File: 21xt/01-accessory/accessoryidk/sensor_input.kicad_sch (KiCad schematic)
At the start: 25 parts, among them IC5 INA821IDGKT, IC6 TXB0108PWR, IC8 INA821IDGKT, IC9 INA821IDGKT, J2 5747847-6, J3 Conn_01x05, J4 Conn_01x06, J5 Conn_01x05, J6 Conn_01x05, J7 Conn_01x06, J8 Conn_01x05

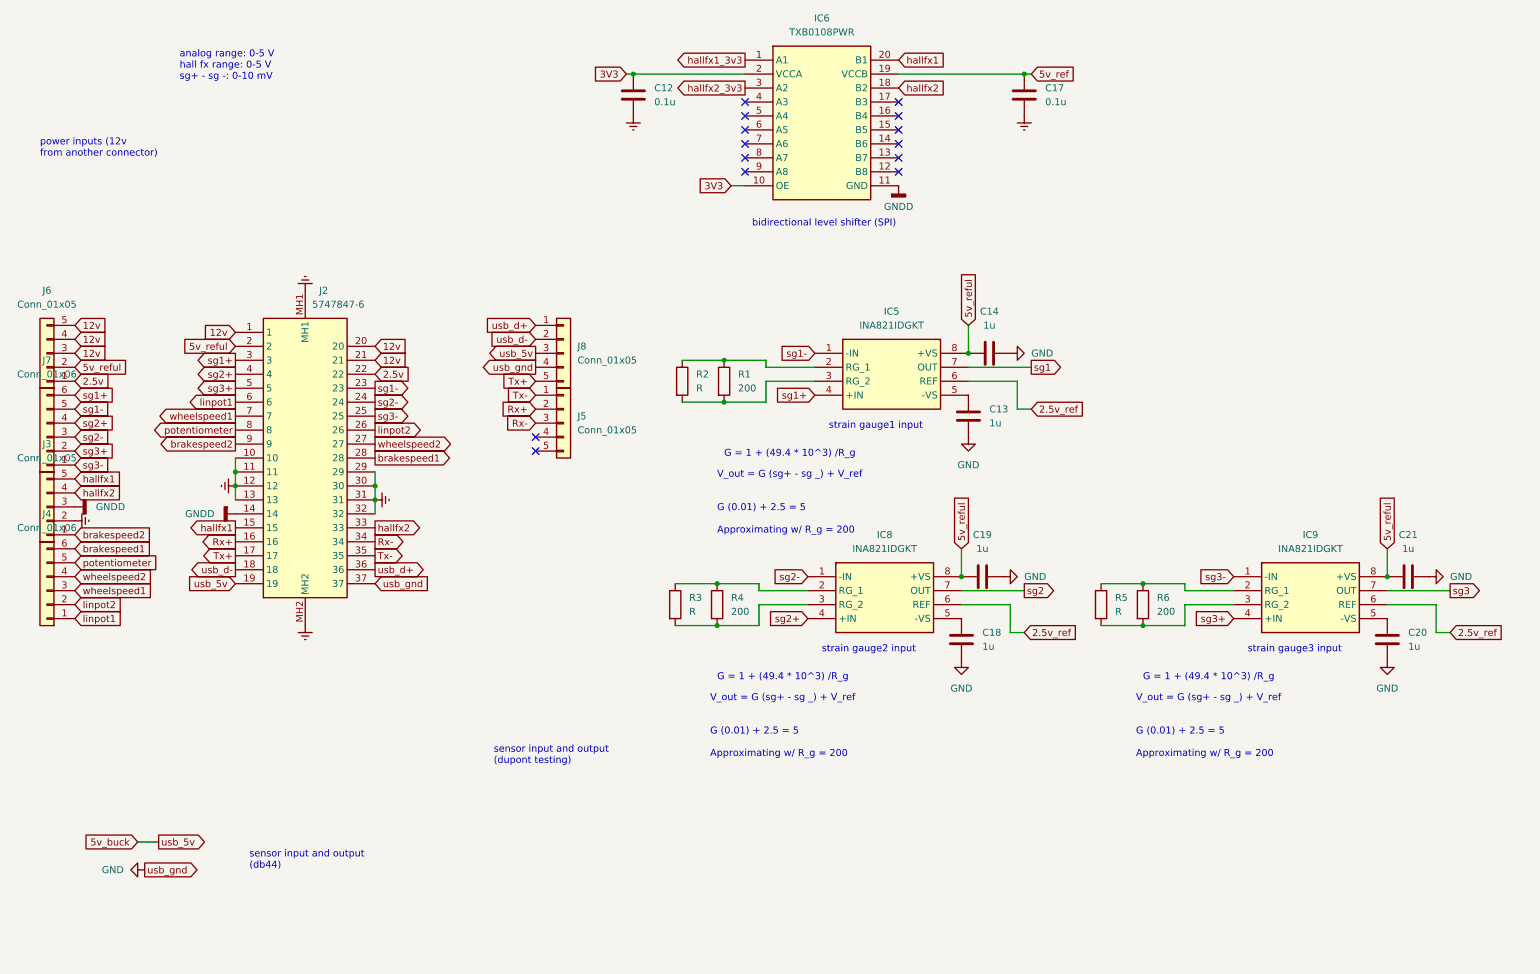
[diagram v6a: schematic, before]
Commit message: Editing V1 accessory layout
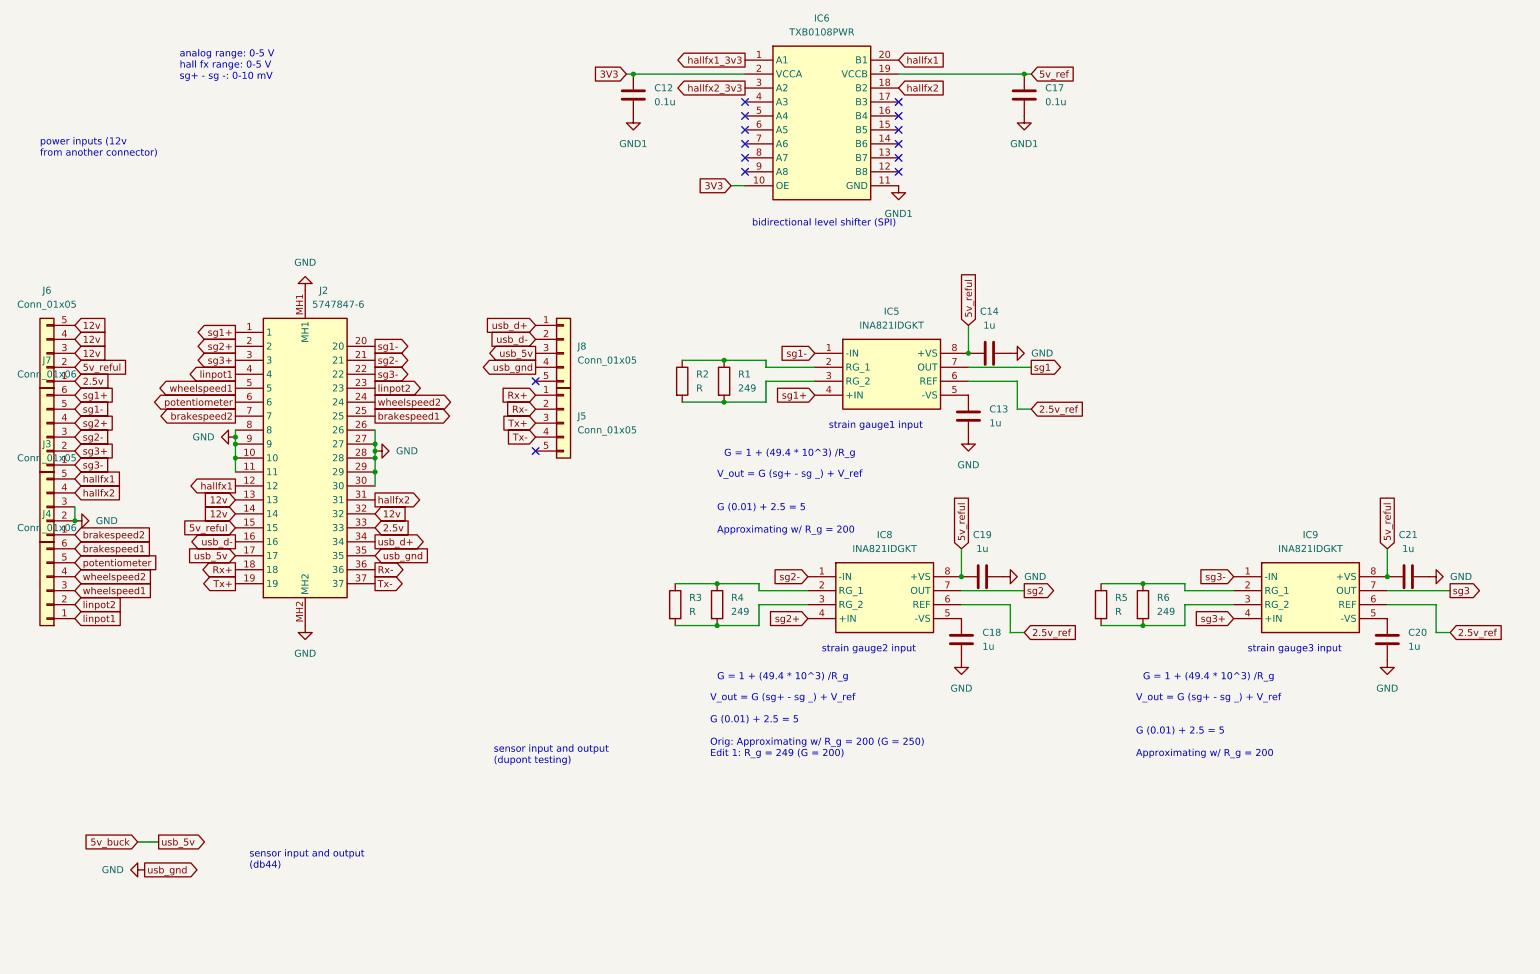
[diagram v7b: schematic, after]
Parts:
- J3, J5, J6, J8: footprint (none) -> Connector_JST:JST_EH_B5B-EH-A_1x05_P2.50mm_Vertical
- J4, J7: footprint (none) -> Connector_JST:JST_EH_B6B-EH-A_1x06_P2.50mm_Vertical
- R1, R4, R6: value 200 -> 249
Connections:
- net 12v: now also J2.13, J2.14, J2.32; no longer J2.1, J2.20, J2.21
- net 2.5v: now also J2.33; no longer J2.22
- net 5v_buck: now also J2.17; no longer J2.19
- net 5v_reful: now also J2.15; no longer J2.2
- net GND: now also J2.10, J2.11, J2.26, J2.27, J2.28, J2.29, J2.30, J2.35, J2.8, J2.9, J2.MH1, J2.MH2, J3.2 (Pin_2), J3.3 (Pin_3); no longer J2.37
- net Rx+: now also J2.18, J5.1 (Pin_1); no longer J2.16, J5.2 (Pin_2)
- net Rx-: now also J2.36, J5.2 (Pin_2); no longer J2.34, J5.3 (Pin_3)
- net Tx+: now also J2.19, J5.3 (Pin_3); no longer J2.17, J8.5 (Pin_5)
- net Tx-: now also J2.37, J5.4 (Pin_4); no longer J2.35, J5.1 (Pin_1)
- net brakespeed1: now also J2.25; no longer J2.28
- net brakespeed2: now also J2.7; no longer J2.9
- net hallfx1: now also J2.12; no longer J2.15
- net hallfx2: now also J2.31; no longer J2.33
- net linpot1: now also J2.4; no longer J2.6
- net linpot2: now also J2.23; no longer J2.26
- net potentiometer: now also J2.6; no longer J2.8
- net sg1+: now also J2.1; no longer J2.3
- net sg1-: now also J2.20; no longer J2.23
- net sg2+: now also J2.2; no longer J2.4
- net sg2-: now also J2.21; no longer J2.24
- net sg3+: now also J2.3; no longer J2.5
- net sg3-: now also J2.22; no longer J2.25
- net usb_d+: now also J2.34; no longer J2.36
- net usb_d-: now also J2.16; no longer J2.18
- net wheelspeed1: now also J2.5; no longer J2.7
- net wheelspeed2: now also J2.24; no longer J2.27
- removed net Earth: C12.2, C17.2, J2.10, J2.11, J2.12, J2.13, J2.29, J2.30, J2.31, J2.32, J2.MH1, J2.MH2, J3.2 (Pin_2)
- removed net GNDD: IC6.11 (GND), J2.14, J3.3 (Pin_3)
- new net GND1: C12.2, C17.2, IC6.11 (GND)
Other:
- note added: "G (0.01) + 2.5 = 5 Orig: Approximating w/ R_g = 200 (G = 250) Edit 1: R_g = 249 (G = 200)"

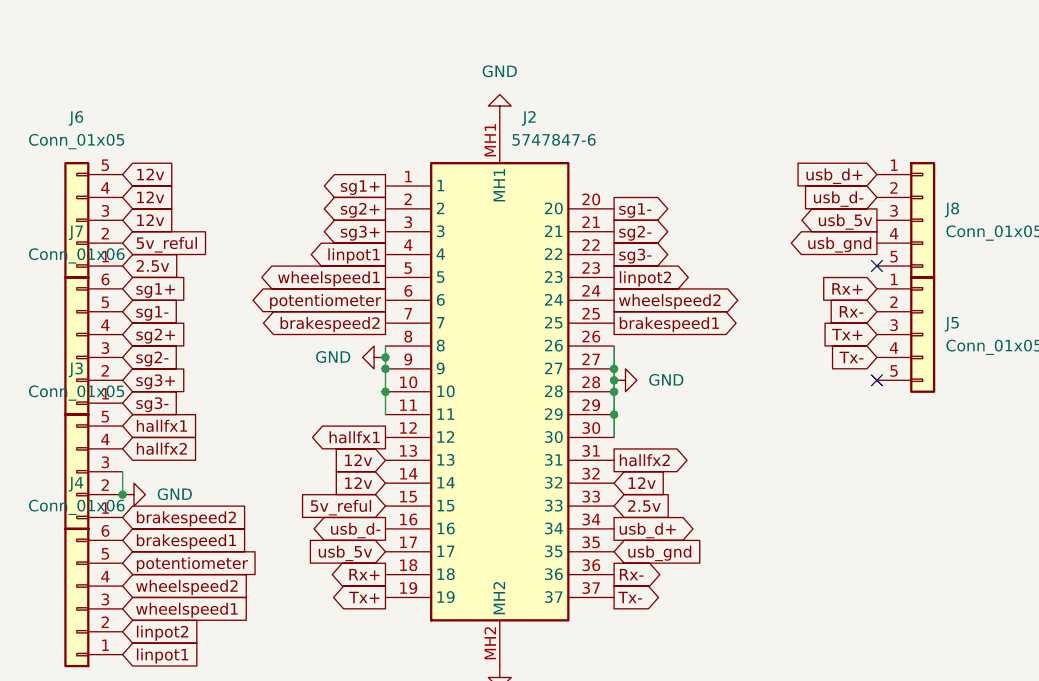
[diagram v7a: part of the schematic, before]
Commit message: FINISHED accessory edited v1 layout, need to check silkscreen
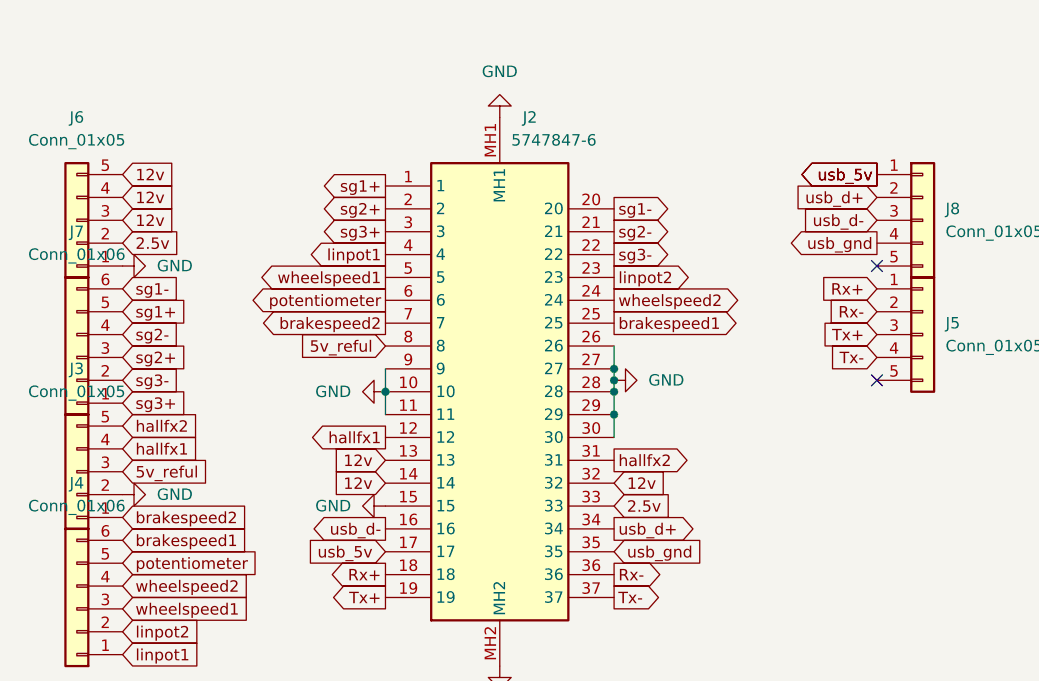
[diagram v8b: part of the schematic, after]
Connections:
- net 2.5v: now also J6.2 (Pin_2); no longer J6.1 (Pin_1)
- net 5v_buck: now also J8.1 (Pin_1); no longer J8.3 (Pin_3)
- net 5v_reful: now also J2.8, J3.3 (Pin_3); no longer J2.15, J6.2 (Pin_2)
- net GND: now also J2.15, J6.1 (Pin_1); no longer J2.8, J3.3 (Pin_3)
- net hallfx1: now also J3.4 (Pin_4); no longer J3.5 (Pin_5)
- net hallfx2: now also J3.5 (Pin_5); no longer J3.4 (Pin_4)
- net sg1+: now also J7.5 (Pin_5); no longer J7.6 (Pin_6)
- net sg1-: now also J7.6 (Pin_6); no longer J7.5 (Pin_5)
- net sg2+: now also J7.3 (Pin_3); no longer J7.4 (Pin_4)
- net sg2-: now also J7.4 (Pin_4); no longer J7.3 (Pin_3)
- net sg3+: now also J7.1 (Pin_1); no longer J7.2 (Pin_2)
- net sg3-: now also J7.2 (Pin_2); no longer J7.1 (Pin_1)
- net usb_d+: now also J8.2 (Pin_2); no longer J8.1 (Pin_1)
- net usb_d-: now also J8.3 (Pin_3); no longer J8.2 (Pin_2)
